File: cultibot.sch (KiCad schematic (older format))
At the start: 34 parts, among them J1 Power, J10 I2C 4, J11 GPIO (NC), J12 ADC (NC), J13 Antenna, J2 Switch 1, J3 Switch 2, J4 Switch 3, J5 Switch 4, J6 I2C 1, J7 I2C 3, J8 Programming, J9 I2C 2, U1 AP2112_K-3.3, U2 ESP8285, Y1 26MHz 10ppm 9pF

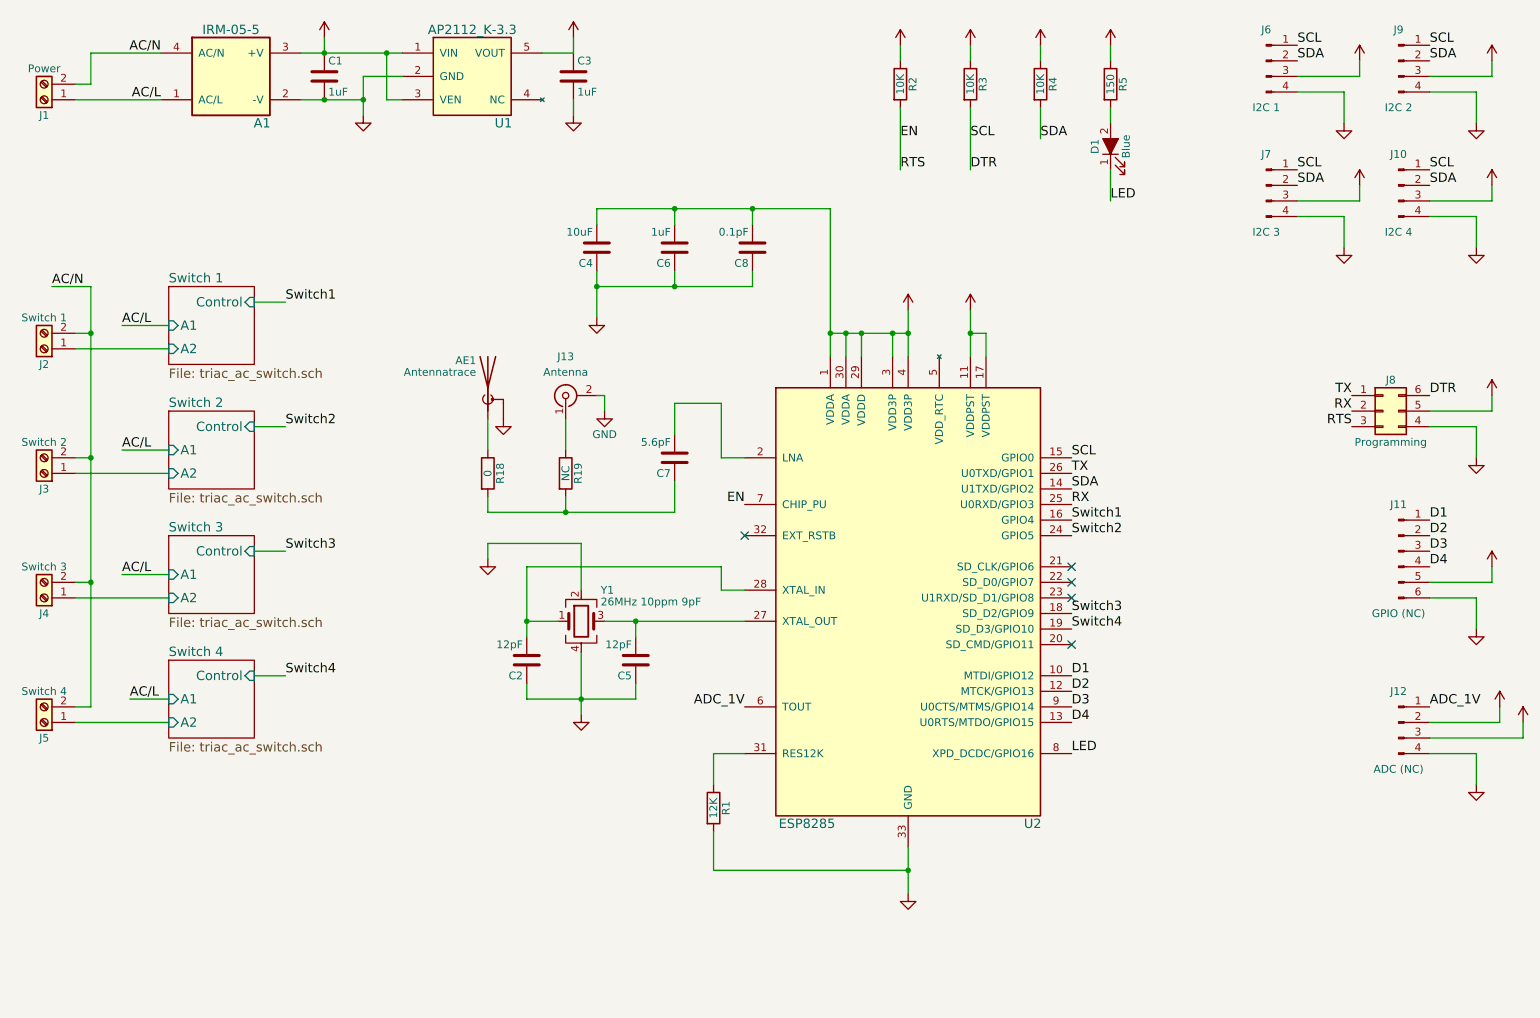
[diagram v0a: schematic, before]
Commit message: 6 output switches, replaced octocoupler
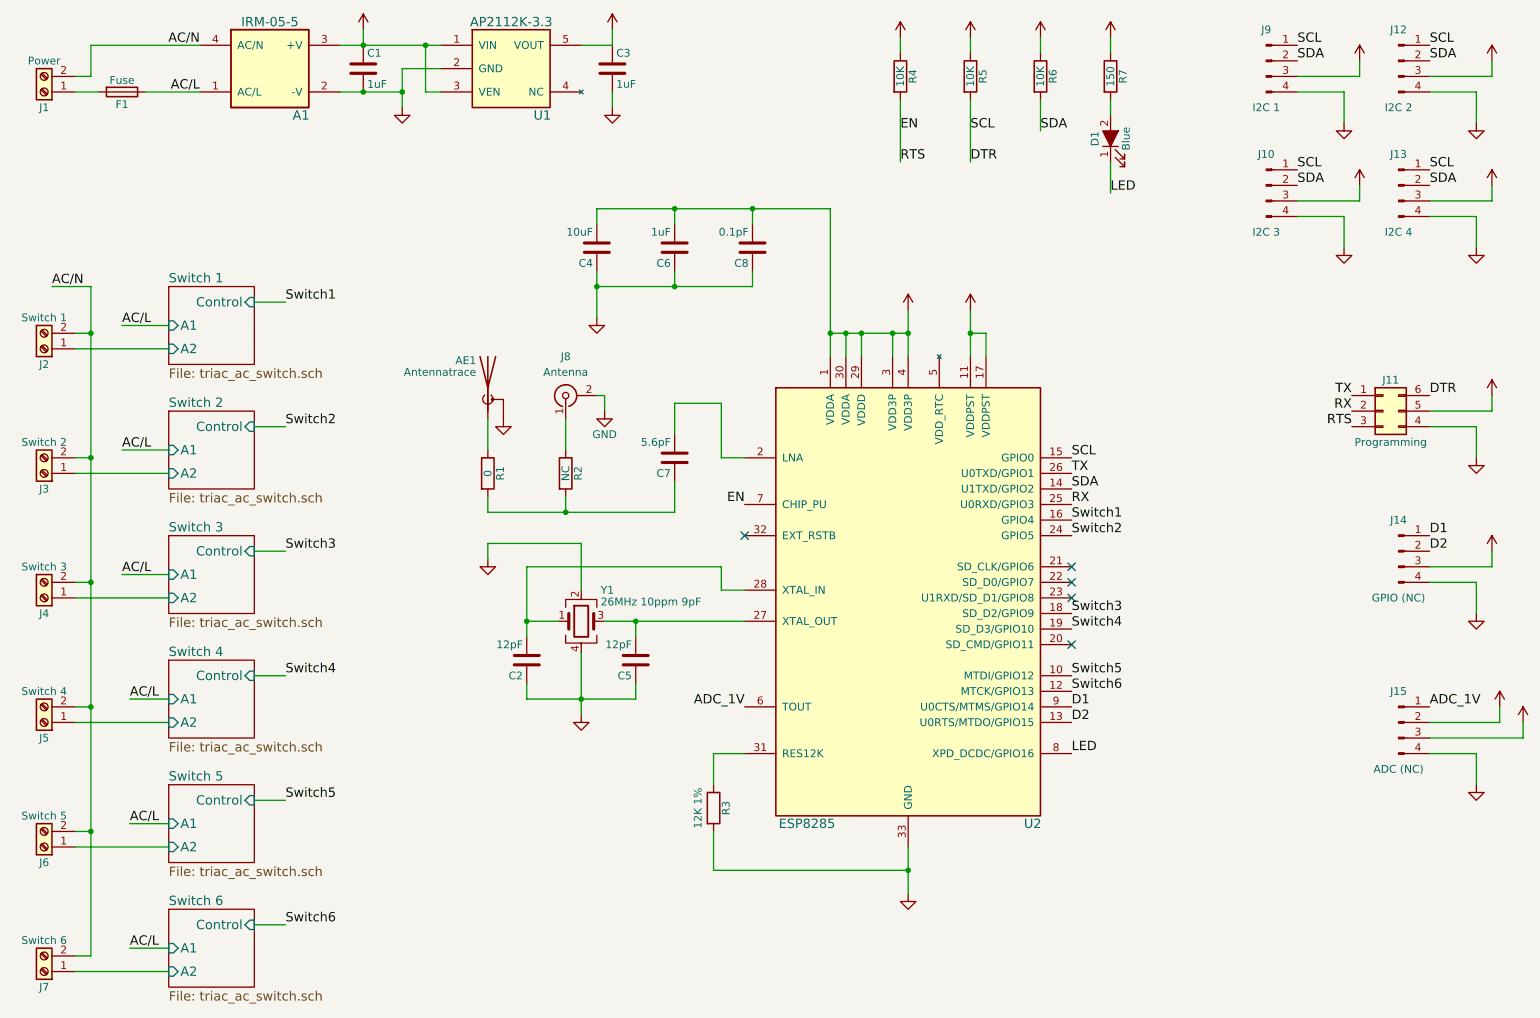
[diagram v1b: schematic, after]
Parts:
- removed J11: GPIO (NC), symbol Conn_01x06_Male
- added F1: Fuse, symbol Fuse
- added J14: GPIO (NC), symbol Conn_01x04_Male
- added J6: Switch 5, symbol Screw_Terminal_01x02
- added J7: Switch 6, symbol Screw_Terminal_01x02
- R3: renamed from R1; value 12K -> 12K 1%
- U1: value AP2112_K-3.3 -> AP2112K-3.3
- renumbered J7 to J10, J8 to J11, J9 to J12, J10 to J13, J12 to J15, J13 to J8, J6 to J9, R18 to R1, R19 to R2, R2 to R4, R3 to R5, R4 to R6, R5 to R7
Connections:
- net D3 is gone; now on net D1: U2.9 (U0CTS/MTMS/GPIO14)
- net D4 is gone; now on net D2: U2.13 (U0RTS/MTDO/GPIO15)
- net +3V3: now also J14.3 (Pin_3)
- net AC/L: now also F1.1; no longer J1.1 (Pin_1)
- net AC/N: now also J6.2 (Pin_2), J7.2 (Pin_2)
- net D1: now also J14.1 (Pin_1); no longer U2.10 (MTDI/GPIO12)
- net D2: now also J14.2 (Pin_2); no longer U2.12 (MTCK/GPIO13)
- net GND: now also J14.4 (Pin_4)
- new net: F1.2, J1.1 (Pin_1)
- new net Switch 5/A2: J6.1 (Pin_1)
- new net Switch 6/A2: J7.1 (Pin_1)
- new net Switch5: U2.10 (MTDI/GPIO12)
- new net Switch6: U2.12 (MTCK/GPIO13)
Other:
- moved on the sheet: A1, C1, C3, D1, J1, R4, R5, R6, R7, U1
